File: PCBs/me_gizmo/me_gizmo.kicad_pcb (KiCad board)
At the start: 2 copper layers, 36 parts, among them J1 Conn_01x06_Pin, J2 Conn_01x24_Pin, J3 Conn_01x09_Pin, U1 ADG714, U2 ADG714, U3 ADG714, U4 ADG714, U5 XS3A4053, U6 XS3A4053

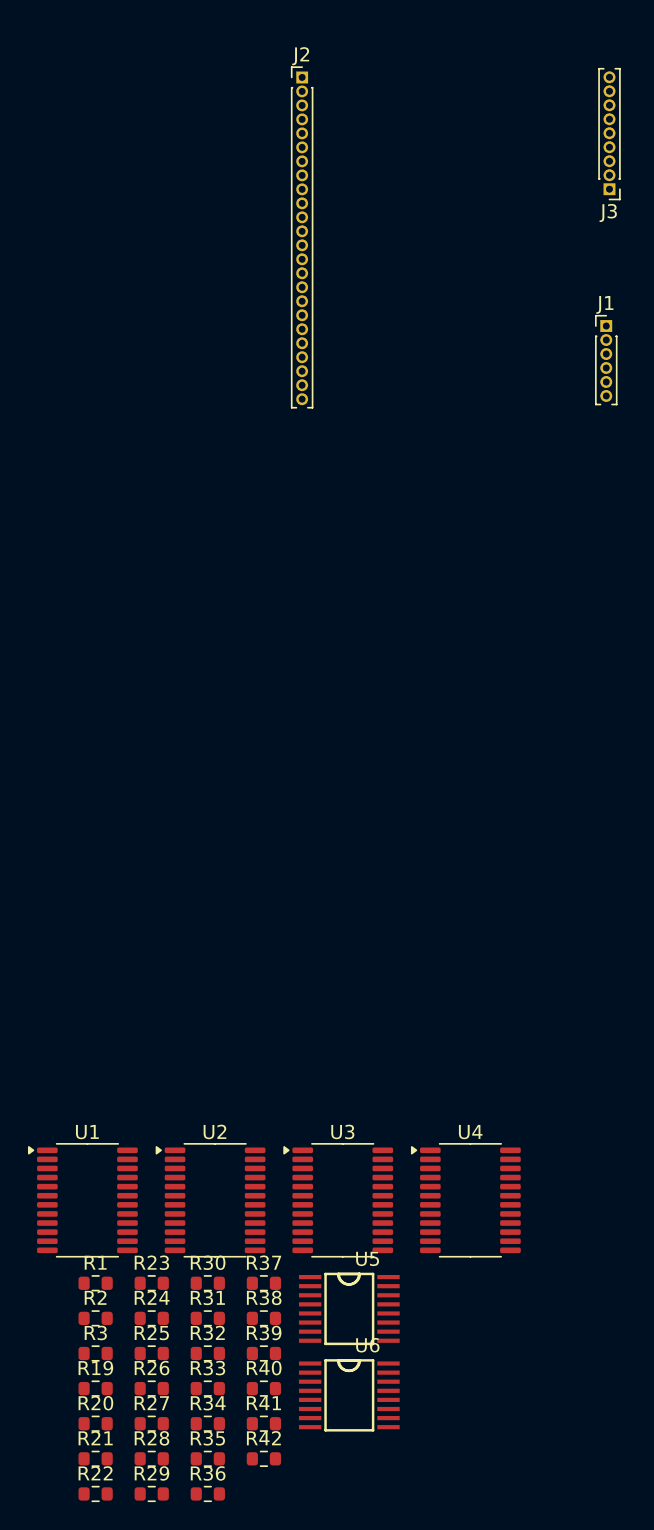
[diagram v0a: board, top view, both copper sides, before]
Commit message: Completed ADG714 Breakout kicad (awaiting further review)
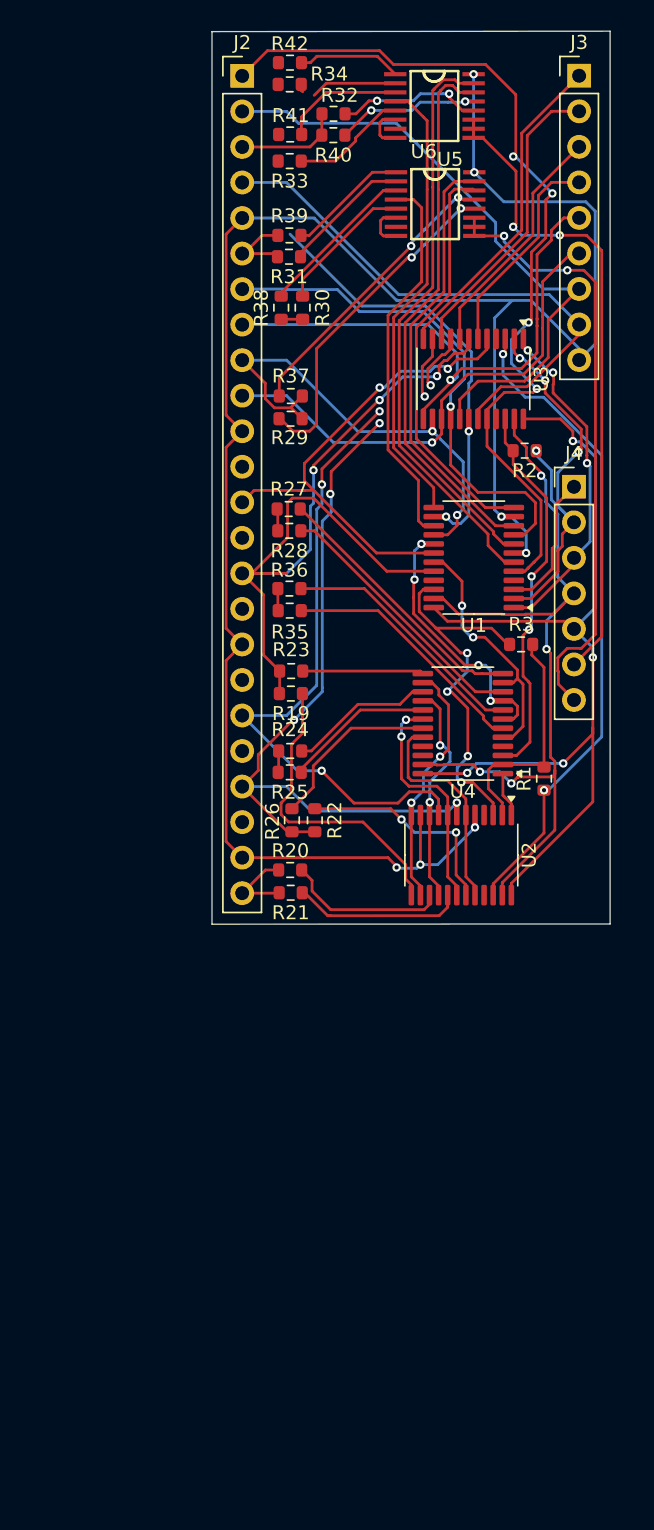
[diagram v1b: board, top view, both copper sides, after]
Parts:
- removed J1: Conn_01x06_Pin, Connector_PinHeader_1.00mm:PinHeader_1x06_P1.00mm_Vertical
- added J4: Conn_01x07_Pin, Connector_PinHeader_2.54mm:PinHeader_1x07_P2.54mm_Vertical, F.Cu at (147.5, 108.8)
- J2: footprint Connector_PinHeader_1.00mm:PinHeader_1x24_P1.00mm_Vertical -> Connector_PinHeader_2.54mm:PinHeader_1x24_P2.54mm_Vertical
- J3: footprint Connector_PinHeader_1.00mm:PinHeader_1x09_P1.00mm_Vertical -> Connector_PinHeader_2.54mm:PinHeader_1x09_P2.54mm_Vertical
- moved R42 99.8 mm to (127.2, 78.4), turned to 180 degrees
- moved R34 95.9 mm to (127.2, 80.0), turned to 180 degrees
- moved U6 92.4 mm to (137.6, 81.5)
- moved R41 92.2 mm to (127.3, 83.6), turned to 180 degrees
- moved R40 89.7 mm to (130.3, 83.6), turned to 180 degrees
- moved R32 89.1 mm to (130.4, 82.1), turned to 180 degrees
- moved R33 87.9 mm to (127.2, 85.5), turned to 180 degrees
- moved R39 79.9 mm to (127.2, 90.8), turned to 180 degrees
- moved U5 79.2 mm to (137.6, 88.5)
- moved R29 77.5 mm to (127.3, 103.9)
- moved R31 76.1 mm to (127.2, 92.3), turned to 180 degrees
- moved R38 72.3 mm to (126.6, 96.0), turned to -90 degrees
- moved R30 70.1 mm to (128.1, 95.9), turned to -90 degrees
- moved R2 69.2 mm to (144.0, 106.2), turned to 180 degrees
- moved R28 67.1 mm to (127.2, 111.9), turned to 180 degrees
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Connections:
- R19 pad 1: unconnected-(R19-Pad1) -> /Wheatstone Bridge 1/RI1
- R23 pad 1: unconnected-(R23-Pad1) -> /Wheatstone Bridge 1/RI2
- U1 pad 10: /Wheatstone Bridge 1/branch3 -> /Wheatstone Bridge 1/branch5
- U1 pad 11: /Wheatstone Bridge 1/HB_OUT2+ -> /Wheatstone Bridge 1/2.5V
- U1 pad 13: /Wheatstone Bridge 1/branch5 -> /Wheatstone Bridge 1/branch3
- U1 pad 14: /Wheatstone Bridge 1/HB_OUT2- -> /Wheatstone Bridge 1/HB_OUT1-
- U1 pad 16: /Wheatstone Bridge 1/2.5V -> /Wheatstone Bridge 1/HB_OUT2-
- U1 pad 6: /Wheatstone Bridge 1/branch1 -> /Wheatstone Bridge 1/branch2
- U1 pad 7: /Wheatstone Bridge 1/HB_OUT1- -> /Wheatstone Bridge 1/2.5V
- U1 pad 8: /Wheatstone Bridge 1/branch2 -> /Wheatstone Bridge 1/branch1
- U1 pad 9: /Wheatstone Bridge 1/2.5V -> /Wheatstone Bridge 1/HB_OUT2+
- U2 pad 10: /Wheatstone Bridge 1/branch11 -> /Wheatstone Bridge 1/branch10
- U2 pad 12: /Wheatstone Bridge 1/branch12 -> /Wheatstone Bridge 1/branch9
- U2 pad 6: /Wheatstone Bridge 1/branch9 -> /Wheatstone Bridge 1/branch12
- U2 pad 7: /Wheatstone Bridge 1/HB_OUT4+ -> /Wheatstone Bridge 1/HB_OUT4-
- U2 pad 8: /Wheatstone Bridge 1/branch10 -> /Wheatstone Bridge 1/branch11
- U2 pad 9: /Wheatstone Bridge 1/HB_OUT4- -> /Wheatstone Bridge 1/HB_OUT4+
- U3 pad 10: /Wheatstone Bridge 1/2ADC_IN3- -> /Wheatstone Bridge 1/2ADC_IN4+
- U3 pad 11: /Wheatstone Bridge 1/HB_OUT3+ -> /Wheatstone Bridge 1/HB_OUT4-
- U3 pad 12: /Wheatstone Bridge 1/2ADC_IN3+ -> /Wheatstone Bridge 1/2ADC_IN4-
- U3 pad 5: /Wheatstone Bridge 1/HB_OUT4- -> /Wheatstone Bridge 1/HB_OUT3+
- U3 pad 6: /Wheatstone Bridge 1/2ADC_IN4- -> /Wheatstone Bridge 1/2ADC_IN3+
- U3 pad 7: /Wheatstone Bridge 1/HB_OUT4+ -> /Wheatstone Bridge 1/HB_OUT3-
- U3 pad 8: /Wheatstone Bridge 1/2ADC_IN4+ -> /Wheatstone Bridge 1/2ADC_IN3-
- U3 pad 9: /Wheatstone Bridge 1/HB_OUT3- -> /Wheatstone Bridge 1/HB_OUT4+
- U4 pad 5: /Wheatstone Bridge 1/branch7 -> /Wheatstone Bridge 1/branch8
- U4 pad 6: /Wheatstone Bridge 1/RG1 -> /Wheatstone Bridge 1/RH1
- U4 pad 7: /Wheatstone Bridge 1/branch8 -> /Wheatstone Bridge 1/branch7
- U4 pad 8: /Wheatstone Bridge 1/RH1 -> /Wheatstone Bridge 1/RG1
- U5 pad 16: unconnected-(U5-VCC-Pad16) -> /Wheatstone Bridge 1/2.5V
- U6 pad 16: unconnected-(U6-VCC-Pad16) -> /Wheatstone Bridge 1/2.5V
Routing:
- net /Wheatstone Bridge 1/2.5V: track 0.00 -> 147.9 mm, vias 0 -> 7
- net /Wheatstone Bridge 1/CS: track 0.00 -> 66.0 mm, vias 0 -> 4
- net /Wheatstone Bridge 1/HB_OUT1+: track 0.00 -> 64.5 mm, vias 0 -> 4
- net /Wheatstone Bridge 1/RESET: track 0.00 -> 60.6 mm, vias 0 -> 4
- net /Wheatstone Bridge 1/HB_OUT3-: track 0.00 -> 59.7 mm, vias 0 -> 3
- net /Wheatstone Bridge 1/HB_OUT4-: track 0.00 -> 58.4 mm, vias 0 -> 5
- net /Wheatstone Bridge 1/HB_OUT4+: track 0.00 -> 50.2 mm, vias 0 -> 4
- net /Wheatstone Bridge 1/VDD: track 0.00 -> 47.6 mm, vias 0 -> 4
- net Net-(U2-DOUT): track 0.00 -> 46.9 mm, vias 0 -> 2
- net /Wheatstone Bridge 1/Rselect1: track 0.00 -> 46.8 mm, vias 0 -> 2
- net /Wheatstone Bridge 1/2ADC_IN1-: track 0.00 -> 44.9 mm
- net /Wheatstone Bridge 1/Rselect2: track 0.00 -> 43.6 mm, vias 0 -> 2
- net /Wheatstone Bridge 1/branch2: track 0.00 -> 41.8 mm
- net /Wheatstone Bridge 1/2ADC_IN2-: track 0.00 -> 41.2 mm, vias 0 -> 1
- net /Wheatstone Bridge 1/HB_OUT1-: track 0.00 -> 40.3 mm, vias 0 -> 2
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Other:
- board outline added: 28.5 x 63.8 mm
